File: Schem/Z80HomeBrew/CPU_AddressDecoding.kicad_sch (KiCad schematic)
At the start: 18 parts, among them U10 ATF22V10C-10PU, U12 74HC273, U19 SST39SF040-70-4C-PHE, U5 Z084000xP, U6 ATF22V10C-10PU, U7 AS7C4096A-12TCN

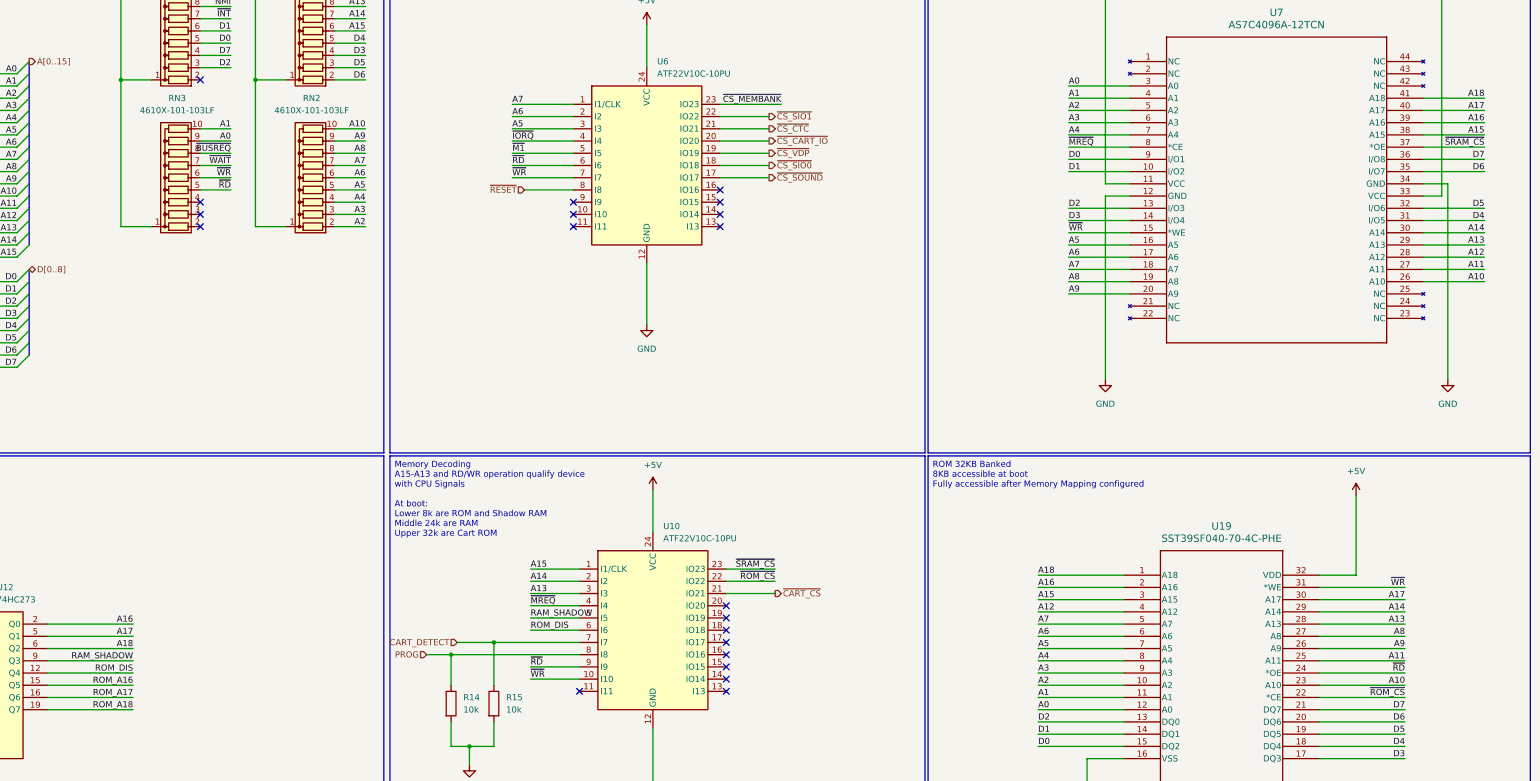
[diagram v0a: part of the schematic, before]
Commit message: Added sound, fixed safe space in memory map, updated CPU address decoding schematic.
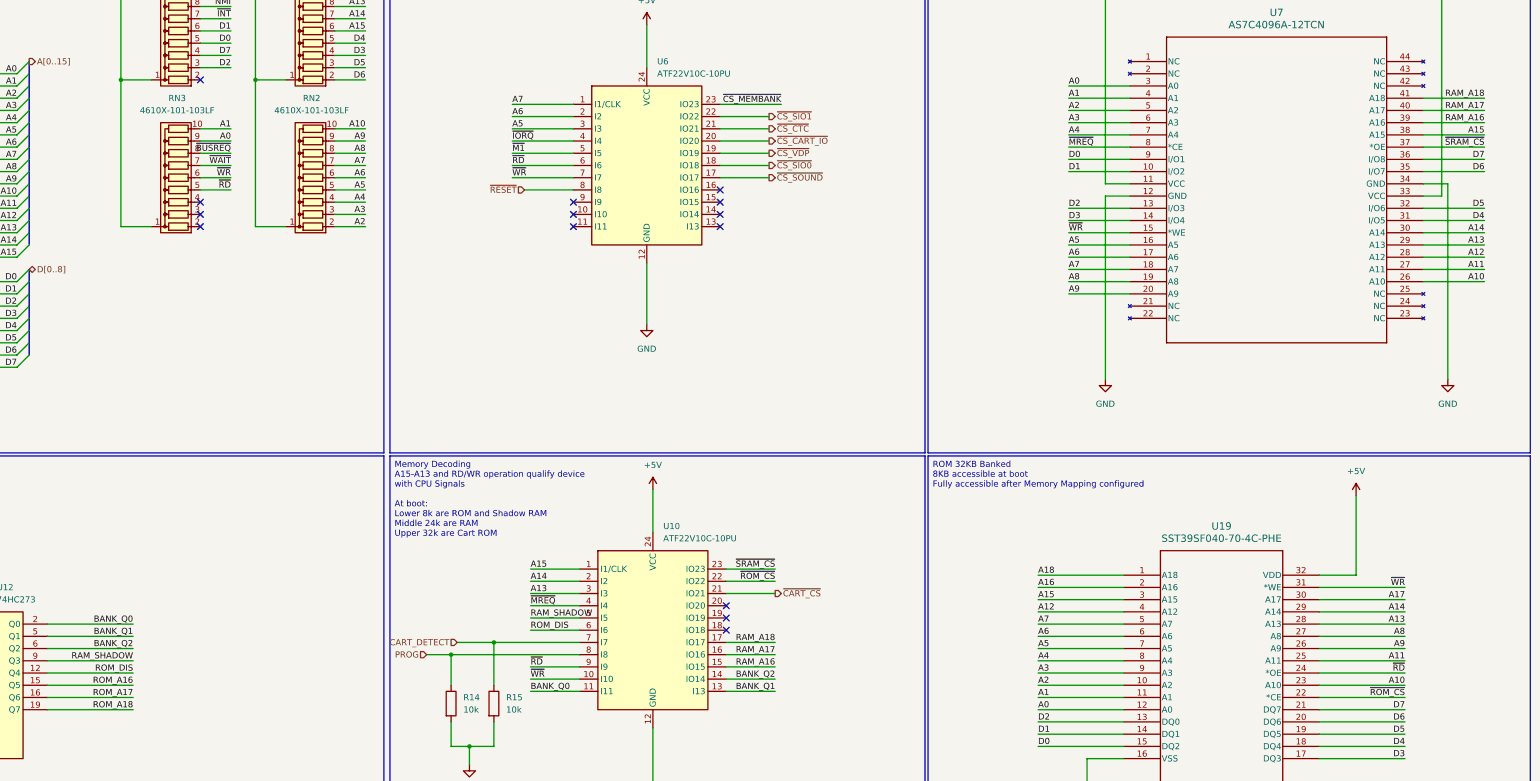
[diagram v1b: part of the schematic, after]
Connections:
- net A16: no longer U12.2 (Q0), U7.39 (A16)
- net A17: no longer U12.5 (Q1), U7.40 (A17)
- net A18: no longer U12.6 (Q2), U7.41 (A18)
- net BANK_Q0: now reaches U10.11 (I11)
- net BANK_Q0: now also U12.2 (Q0)
- net BANK_Q1: now reaches U10.13 (I13)
- net BANK_Q1: now also U12.5 (Q1)
- net BANK_Q2: now reaches U10.14 (IO14)
- net BANK_Q2: now also U12.6 (Q2)
- net RAM_A16: now reaches U10.15 (IO15)
- net RAM_A16: now also U7.39 (A16)
- net RAM_A17: now reaches U10.16 (IO16)
- net RAM_A17: now also U7.40 (A17)
- net RAM_A18: now reaches U10.17 (IO17)
- net RAM_A18: now also U7.41 (A18)
- no-connect marks 21 -> 15
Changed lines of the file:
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@@
 	)
 	(no_connect
-		(at 200.66 177.8)
-	)
-	(no_connect
 		(at 199.39 81.28)
 	)
@@
 	)
 	(no_connect
-		(at 231.14 167.64)
-	)
-	(no_connect
-		(at 231.14 172.72)
-	)
-	(no_connect
 		(at 229.87 78.74)
 	)
@@
 	)
 	(no_connect
-		(at 231.14 177.8)
-	)
-	(no_connect
 		(at 44.45 74.93)
 	)
@@
 	)
 	(no_connect
-		(at 231.14 170.18)
-	)
-	(no_connect
 		(at 229.87 73.66)
 	)
@@
 		(at 121.92 81.28)
 	)
-	(no_connect
-		(at 231.14 175.26)
-	)
 	(bus_entry
 		(at 83.82 105.41)
@@
 		)
 	)
+	(wire
+		(pts
+			(xy 190.5 177.8) (xy 200.66 177.8)
+		)
+		(stroke
+			(width 0)
+			(type default)
+		)
+	)
 	(bus
 		(pts
@@
 	(wire
 		(pts
+			(xy 231.14 172.72) (xy 241.3 172.72)
+		)
+		(stroke
+			(width 0)
+			(type default)
+		)
+	)
+	(wire
+		(pts
 			(xy 190.5 154.94) (xy 200.66 154.94)
 		)
@@
 	(wire
 		(pts
+			(xy 231.14 177.8) (xy 241.3 177.8)
+		)
+		(stroke
+			(width 0)
+			(type default)
+		)
+	)
+	(wire
+		(pts
 			(xy 354.33 166.37) (xy 372.11 166.37)
 		)
@@
 	(wire
 		(pts
+			(xy 231.14 175.26) (xy 241.3 175.26)
+		)
+		(stroke
+			(width 0)
+			(type default)
+		)
+	)
+	(wire
+		(pts
 			(xy 69.85 54.61) (xy 83.82 54.61)
 		)
@@
 	(wire
 		(pts
+			(xy 231.14 167.64) (xy 241.3 167.64)
+		)
+		(stroke
+			(width 0)
+			(type default)
+		)
+	)
+	(wire
+		(pts
 			(xy 186.69 66.04) (xy 199.39 66.04)
 		)
@@
 	(wire
 		(pts
+			(xy 231.14 170.18) (xy 241.3 170.18)
+		)
+		(stroke
+			(width 0)
+			(type default)
+		)
+	)
+	(wire
+		(pts
 			(xy 121.92 43.18) (xy 128.27 43.18)
 		)
@@
 		)
 	)
-	(label "A17"
+	(label "BANK_Q1"
 		(at 107.95 166.37 180)
 		(effects
@@
 		)
 	)
-	(label "A16"
+	(label "BANK_Q0"
 		(at 107.95 163.83 180)
 		(effects
@@
 		)
 	)
+	(label "RAM_A17"
+		(at 241.3 170.18 180)
+		(effects
+			(font
+				(size 1.27 1.27)
+			)
+			(justify right bottom)
+		)
+	)
 	(label "A12"
 		(at 388.62 87.63 180)
@@
 		)
 	)
-	(label "A18"
-		(at 388.62 54.61 180)
-		(effects
-			(font
-				(size 1.27 1.27)
-			)
-			(justify right bottom)
-		)
-	)
-	(label "A18"
+	(label "BANK_Q2"
 		(at 107.95 168.91 180)
 		(effects
@@
 		)
 	)
-	(label "A16"
-		(at 388.62 59.69 180)
-		(effects
-			(font
-				(size 1.27 1.27)
-			)
-			(justify right bottom)
-		)
-	)
 	(label "~{NMI}"
 		(at 30.48 95.25 0)
@@
 		)
 	)
+	(label "RAM_A18"
+		(at 388.62 54.61 180)
+		(effects
+			(font
+				(size 1.27 1.27)
+			)
+			(justify right bottom)
+		)
+	)
 	(label "D6"
 		(at 50.8 179.07 0)
@@
 		)
 	)
+	(label "RAM_A17"
+		(at 388.62 57.15 180)
+		(effects
+			(font
+				(size 1.27 1.27)
+			)
+			(justify right bottom)
+		)
+	)
 	(label "A13"
 		(at 156.21 35.56 180)
@@
 		)
 	)
+	(label "BANK_Q2"
+		(at 241.3 175.26 180)
+		(effects
+			(font
+				(size 1.27 1.27)
+			)
+			(justify right bottom)
+		)
+	)
 	(label "A3"
 		(at 302.26 59.69 0)
@@
 		)
 	)
+	(label "RAM_A16"
+		(at 388.62 59.69 180)
+		(effects
+			(font
+				(size 1.27 1.27)
+			)
+			(justify right bottom)
+		)
+	)
 	(label "A6"
 		(at 186.69 58.42 0)
@@
 		)
 	)
+	(label "BANK_Q0"
+		(at 190.5 177.8 0)
+		(effects
+			(font
+				(size 1.27 1.27)
+			)
+			(justify left bottom)
+		)
+	)
 	(label "A9"
 		(at 372.11 168.91 180)
@@
 		)
 	)
+	(label "BANK_Q1"
+		(at 241.3 177.8 180)
+		(effects
+			(font
+				(size 1.27 1.27)
+			)
+			(justify right bottom)
+		)
+	)
 	(label "D2"
 		(at 302.26 77.47 0)
@@
 		)
 	)
+	(label "RAM_A16"
+		(at 241.3 172.72 180)
+		(effects
+			(font
+				(size 1.27 1.27)
+			)
+			(justify right bottom)
+		)
+	)
 	(label "A4"
 		(at 83.82 59.69 180)
@@
 		)
 	)
-	(label "A17"
-		(at 388.62 57.15 180)
+	(label "RAM_A18"
+		(at 241.3 167.64 180)
 		(effects
 			(font
